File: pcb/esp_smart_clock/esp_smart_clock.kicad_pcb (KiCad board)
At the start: 2 copper layers, 95 x 54 mm, 108 parts, among them IC1 CR1220-2, J1 Connector, USB-TYPE-C-16P, J10 MTLW-101-05-G-D-150, J11 MTLW-101-05-G-D-150, J14 MTLW-101-05-G-D-150, J15 MTLW-101-05-G-D-150, J16 MTLW-101-05-G-D-150, J17 MTLW-101-05-G-D-150, J18 MTLW-101-05-G-D-150, J19 MTLW-101-05-G-D-150, J2 MTLW-101-05-G-D-150, J20 MTLW-101-05-G-D-150, J22 MTLW-101-05-G-D-150, J23 MTLW-101-05-G-D-150, J24 MTLW-101-05-G-D-150, J3 MTLW-101-05-G-D-150, J4 MTLW-101-05-G-D-150, J5 MTLW-101-05-G-D-150, J6 MTLW-101-05-G-D-150, J7 MTLW-101-05-G-D-150, J8 MTLW-101-05-G-D-150, J9 MTLW-101-05-G-D-150, P1 PHR-2, P2 PHR-2, P3 PHR-2, Q1 S8050, Q2 S8050, Q3 S8050, Q4 S8050, U1 ESP32-WROOM-32D-N4, U2 AMS1117-3.3, U3 TP4056, U4 PCF8563T, U8 CH340K, X1 Q13FC1350000400

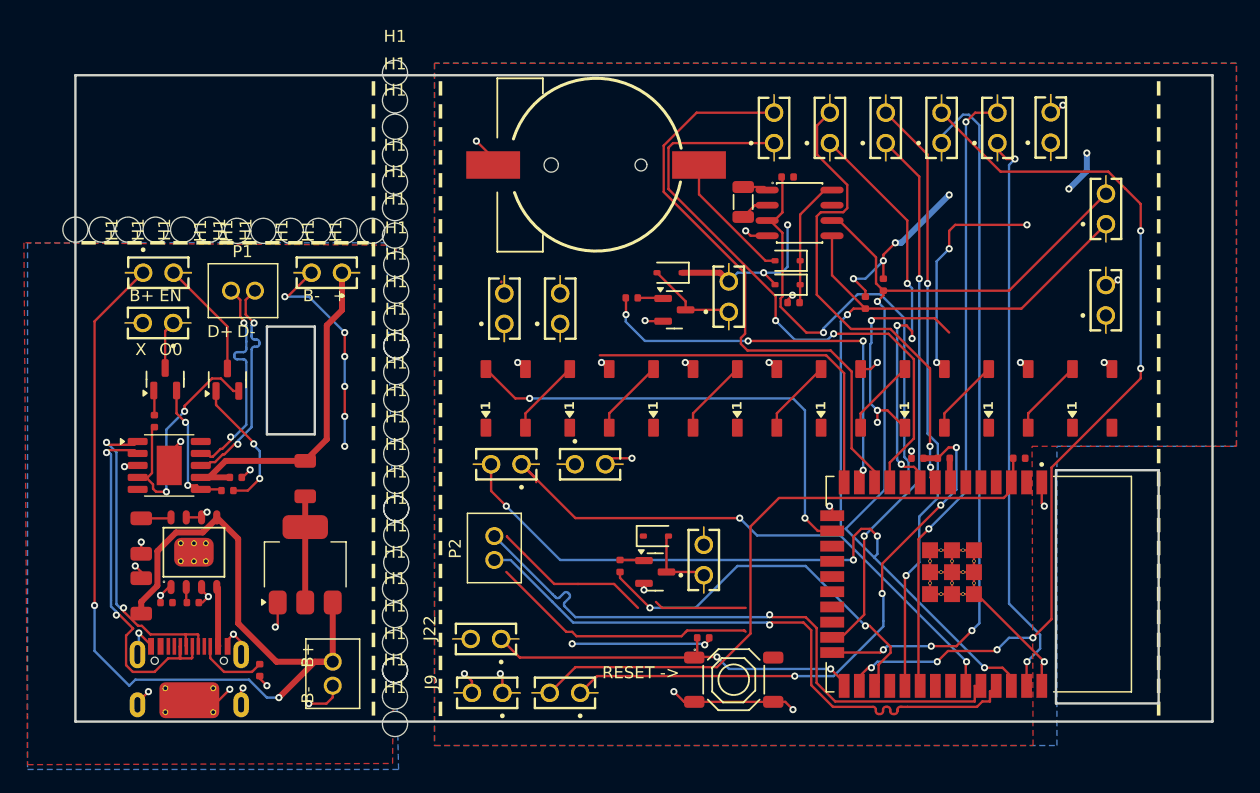
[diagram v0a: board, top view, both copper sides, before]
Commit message: Update README and PCB files, add SD card subproject
Updated the README with new ESP32 module info, BOM clarifications, and added a gallery section. Removed outdated PCB autosave and backup files, added new SD card KiCad project files, and updated main PCB and schematic files to reflect recent hardware changes.
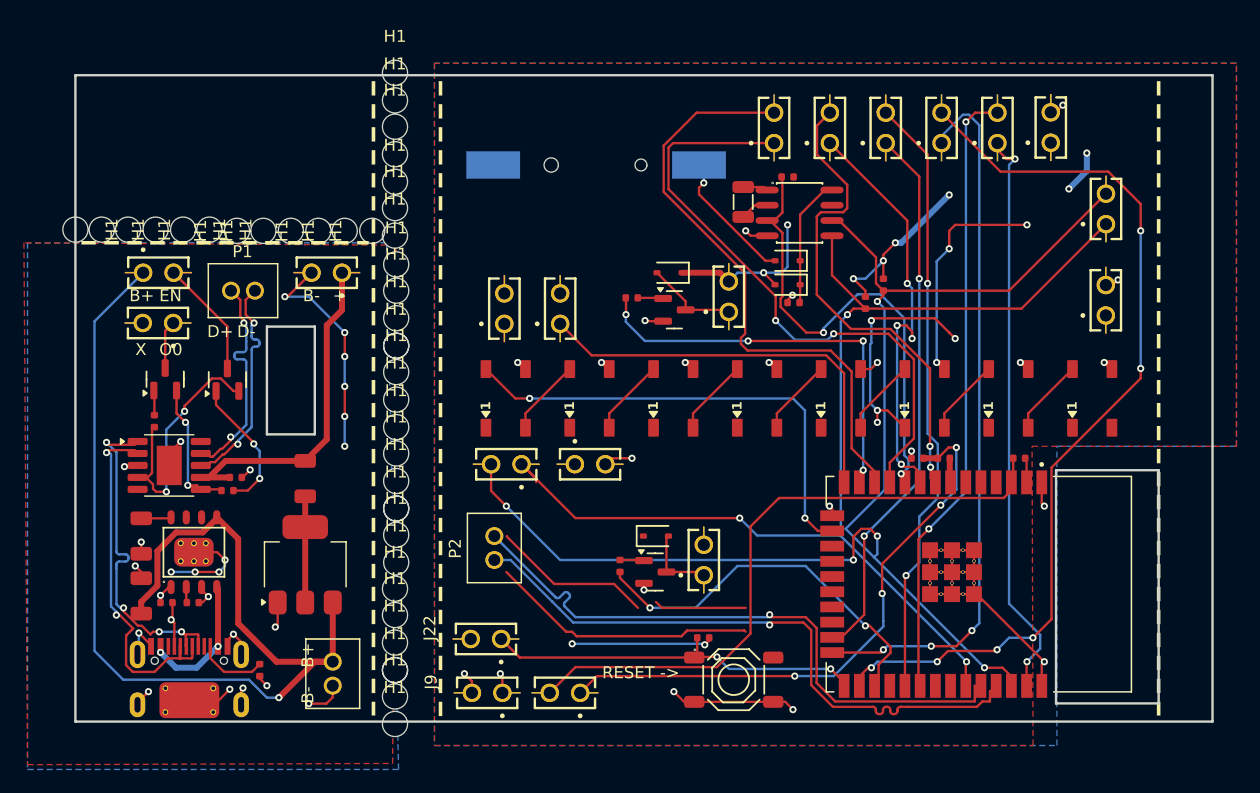
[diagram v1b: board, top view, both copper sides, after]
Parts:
- IC1: moved to B.Cu
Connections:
- U3 pad 6: GND -> unconnected-(U3-STDBY#-Pad6)
- U3 pad 7: GND -> unconnected-(U3-CHRG#-Pad7)
- U3 pad 9: unconnected-(U3-EP-Pad9)_4 -> GND
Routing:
- net VBUS: track 7.57 -> 14.1 mm, vias 0 -> 2
- net IO12: track 30.2 -> 34.6 mm
- net Net-(J1-CC1): track 0.00 -> 3.81 mm, vias 0 -> 1
- net GND: track 136.5 -> 140.1 mm, vias 47 -> 49
- net +3V3: track 93.7 -> 96.5 mm, vias 14 -> 15
- net USB_D+: track 26.7 -> 28.4 mm, vias 2 -> 4
- net B+: track 140.9 -> 140.5 mm, vias 6 -> 5
- net IO25: track 40.0 -> 40.4 mm, vias 1 -> 2
- net COIN+: track 11.1 -> 11.4 mm, vias 0 -> 1
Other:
- board text removed: "Teď se modlit aby to fungovalo - Martin Šrámek"

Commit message: Remove D2 diode and update net assignments
Removed the D2 (1N4148WS) diode footprint from the PCB design and updated net assignments throughout the esp_smart_clock.kicad_pcb file to reflect the change. Also updated backup files and made minor netlist adjustments, marking IO14 and IO16 as unconnected. Deleted old backup files and added new ones.
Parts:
- removed D10, D2: 1N4148WS, PCM_JLCPCB:D_SOD-323
- removed J14, J24: MTLW-101-05-G-D-150, footprints:SAMTEC_MTLW-101-05-G-D-150
- removed Q1, Q4: S8050, PCM_JLCPCB:Q_SOT-23
- removed R7, R8: 1.2kΩ, PCM_JLCPCB:R_0402
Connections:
- U1 pad 13: IO14 -> unconnected-(U1-IO14-Pad13)
- U1 pad 27: IO16 -> unconnected-(U1-IO16-Pad27)
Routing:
- net IO14: track 34.5 -> 0.00 mm, vias 4 -> 0
- net IO16: track 32.2 -> 0.00 mm, vias 2 -> 0
- net VIB-: track 7.77 -> 0.00 mm
- net BUZ-: track 6.30 -> 0.00 mm
- net (no net): track 43.6 -> 47.4 mm
- net +3V3: track 96.5 -> 93.3 mm, vias 15 -> 16
- net Net-(Q1-B): track 2.14 -> 0.00 mm
- net GND: track 140.1 -> 138.0 mm, vias 49 -> 47
- net Net-(Q4-B): track 2.02 -> 0.00 mm
- net unconnected-(U1-IO14-Pad13): track 0.00 -> 0.70 mm
